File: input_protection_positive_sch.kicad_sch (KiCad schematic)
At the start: 25 parts, among them Q1 SQM120P06, Q2 SQM120P06, U1 ADM1270

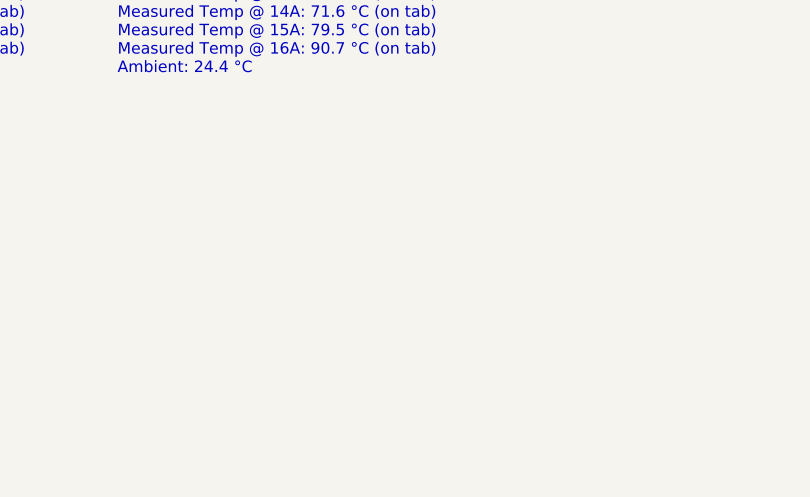
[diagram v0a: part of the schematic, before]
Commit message: Only run pre-commit hooks in the datasheet dir
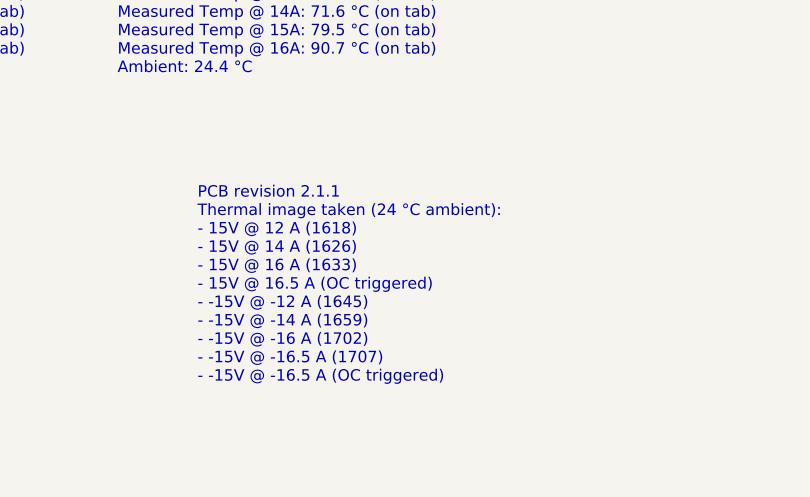
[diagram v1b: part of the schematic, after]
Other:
- note added: "PCB revision 2.1.1 Thermal image taken (24 °C ambient): - 15V @ 12 A (1618) - 15V @ 14 A (1626) - 15V @ 16 A (1633) - 15V @ 16.5 A (OC triggered) - -15V @ -12 A (1645) - -15V @ -14 A (1659) - -15V @ -16 A (1702) - -15V @ -16.5 A (1707) - -15V @ -16.5 A (OC triggered)"
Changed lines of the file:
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@@
+		)
+	)
+	(text "PCB revision 2.1.1\nThermal image taken (24 °C ambient):\n- 15V @ 12 A (1618)\n- 15V @ 14 A (1626)\n- 15V @ 16 A (1633)\n- 15V @ 16.5 A (OC triggered)\n- -15V @ -12 A (1645)\n- -15V @ -14 A (1659)\n- -15V @ -16 A (1702)\n- -15V @ -16.5 A (1707)\n- -15V @ -16.5 A (OC triggered)"
+		(exclude_from_sim no)
+		(at 101.6 180.34 0)
+		(effects
+			(font
+				(size 1.27 1.27)
+			)
+			(justify left bottom)
 		)
 	)

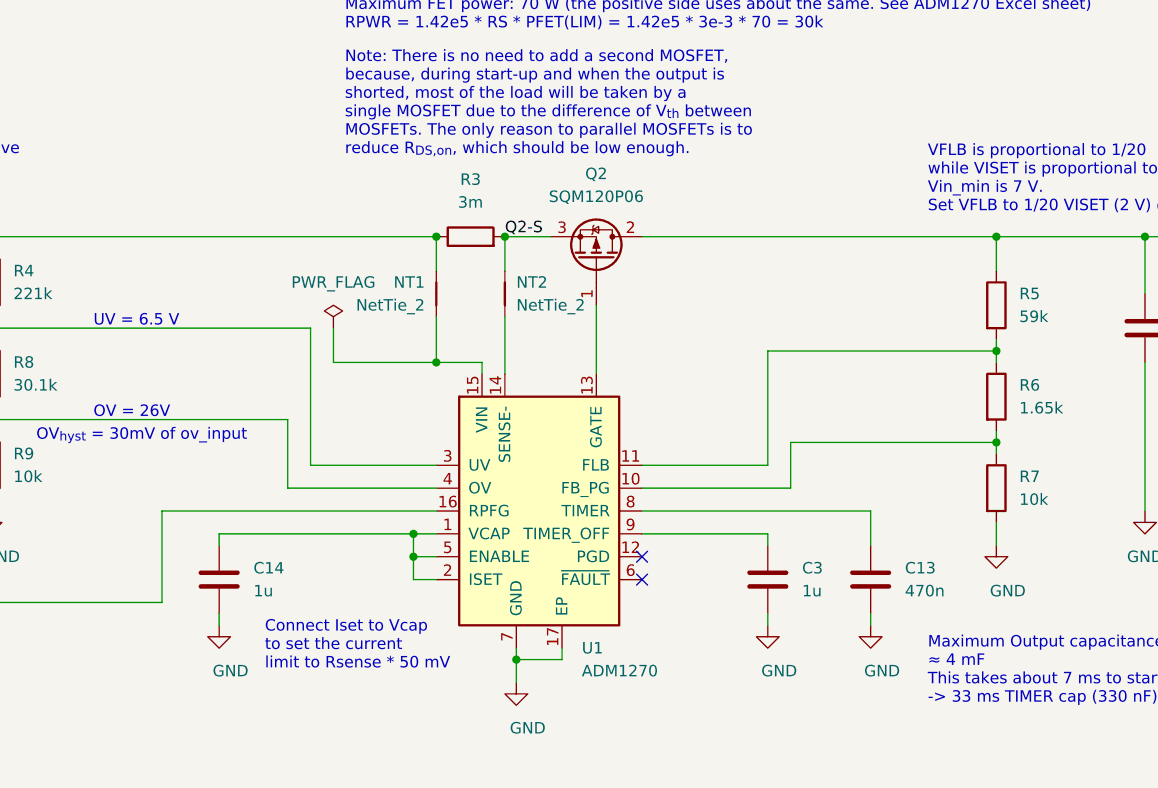
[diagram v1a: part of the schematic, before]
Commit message: Updated libraries
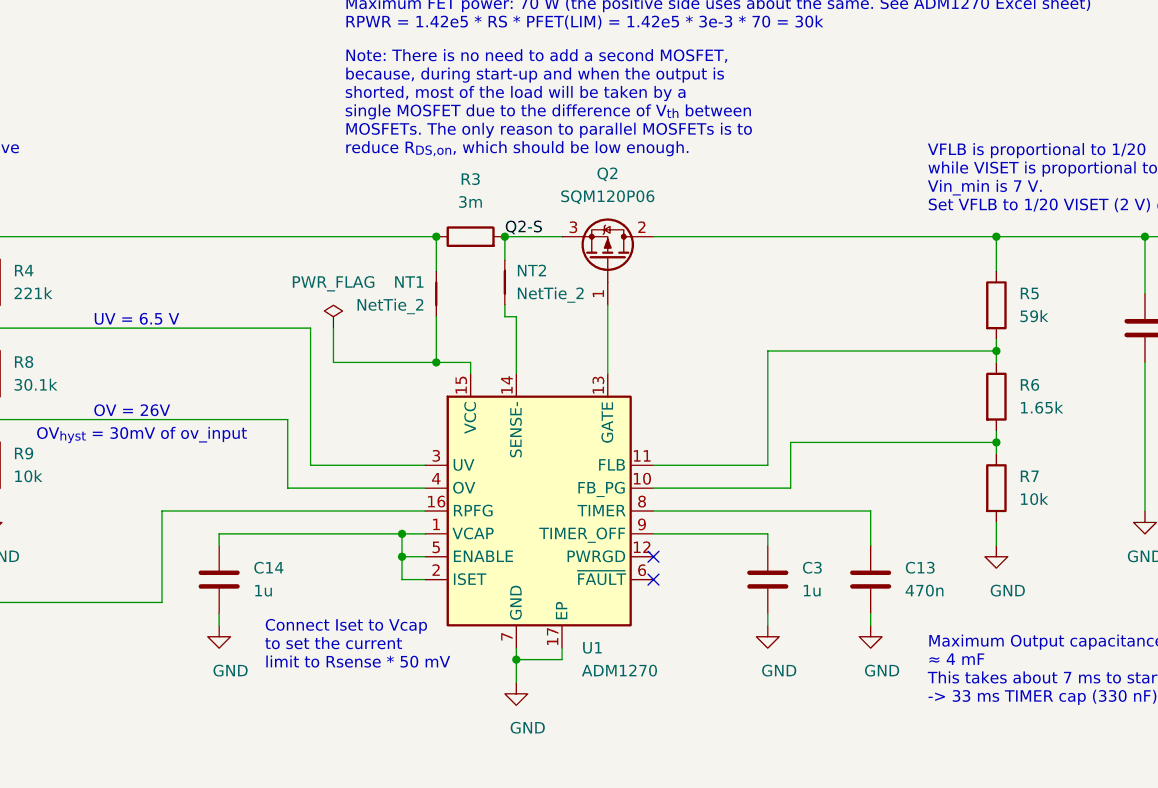
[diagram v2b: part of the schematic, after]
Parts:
- U1: footprint Package_DFN_QFN:QFN-16-1EP_3x3mm_P0.5mm_EP1.45x1.45mm -> Package_CSP:LFCSP-16-1EP_3x3mm_P0.5mm_EP1.5x1.5mm; symbol ADI:ADM1270ACPZ -> Power_Management:ADM1270ACPZ
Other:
- moved on the sheet: NT2, Q2
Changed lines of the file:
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@@
 	)
 	(junction
-		(at 163.83 100.33)
+		(at 162.56 100.33)
 		(diameter 0)
 		(color 0 0 0 0)
@@
 	)
 	(junction
-		(at 163.83 97.79)
+		(at 162.56 97.79)
 		(diameter 0)
 		(color 0 0 0 0)
@@
 	)
 	(no_connect
-		(at 189.23 102.87)
+		(at 190.5 102.87)
 	)
 	(no_connect
-		(at 189.23 100.33)
+		(at 190.5 100.33)
 	)
 	(wire
 		(pts
-			(xy 163.83 100.33) (xy 163.83 102.87)
+			(xy 162.56 100.33) (xy 162.56 102.87)
 		)
 		(stroke
@@
 	(wire
 		(pts
-			(xy 189.23 97.79) (xy 203.2 97.79)
+			(xy 190.5 97.79) (xy 203.2 97.79)
 		)
 		(stroke
@@
 	(wire
 		(pts
-			(xy 163.83 102.87) (xy 166.37 102.87)
+			(xy 162.56 102.87) (xy 165.1 102.87)
 		)
 		(stroke
@@
 	(wire
 		(pts
-			(xy 173.99 64.77) (xy 173.99 68.58)
+			(xy 173.99 64.77) (xy 173.99 67.31)
 		)
 		(stroke
@@
 	(wire
 		(pts
-			(xy 163.83 97.79) (xy 163.83 100.33)
+			(xy 162.56 97.79) (xy 162.56 100.33)
 		)
 		(stroke
@@
 	(wire
 		(pts
-			(xy 173.99 73.66) (xy 173.99 80.01)
+			(xy 175.26 73.66) (xy 175.26 80.01)
 		)
 		(stroke
@@
 	(wire
 		(pts
-			(xy 166.37 92.71) (xy 149.86 92.71)
+			(xy 165.1 92.71) (xy 149.86 92.71)
 		)
 		(stroke
@@
 	(wire
 		(pts
+			(xy 175.26 73.66) (xy 173.99 73.66)
+		)
+		(stroke
+			(width 0)
+			(type default)
+		)
+	)
+	(wire
+		(pts
 			(xy 149.86 85.09) (xy 116.84 85.09)
 		)
@@
 	(wire
 		(pts
-			(xy 189.23 95.25) (xy 214.63 95.25)
+			(xy 190.5 95.25) (xy 214.63 95.25)
 		)
 		(stroke
@@
 	(wire
 		(pts
-			(xy 142.24 97.79) (xy 163.83 97.79)
+			(xy 142.24 97.79) (xy 162.56 97.79)
 		)
 		(stroke
@@
 	(wire
 		(pts
-			(xy 166.37 78.74) (xy 171.45 78.74)
+			(xy 166.37 78.74) (xy 170.18 78.74)
 		)
 		(stroke
@@
 	(wire
 		(pts
-			(xy 166.37 100.33) (xy 163.83 100.33)
+			(xy 165.1 100.33) (xy 162.56 100.33)
 		)
 		(stroke
@@
 	(wire
 		(pts
-			(xy 259.08 74.93) (xy 259.08 76.2)
+			(xy 170.18 78.74) (xy 170.18 80.01)
 		)
 		(stroke
@@
 	(wire
 		(pts
-			(xy 228.6 64.77) (xy 245.11 64.77)
+			(xy 173.99 73.66) (xy 173.99 72.39)
 		)
 		(stroke
@@
 	(wire
 		(pts
-			(xy 228.6 77.47) (xy 203.2 77.47)
+			(xy 259.08 74.93) (xy 259.08 76.2)
 		)
 		(stroke
@@
 	(wire
 		(pts
-			(xy 166.37 78.74) (xy 154.94 78.74)
+			(xy 228.6 64.77) (xy 245.11 64.77)
 		)
 		(stroke
@@
 	(wire
 		(pts
-			(xy 163.83 97.79) (xy 166.37 97.79)
+			(xy 228.6 77.47) (xy 203.2 77.47)
 		)
 		(stroke
@@
 	(wire
 		(pts
-			(xy 116.84 73.66) (xy 116.84 74.93)
+			(xy 166.37 78.74) (xy 154.94 78.74)
 		)
 		(stroke
@@
 	(wire
 		(pts
-			(xy 203.2 90.17) (xy 189.23 90.17)
+			(xy 162.56 97.79) (xy 165.1 97.79)
 		)
 		(stroke
@@
 	(wire
 		(pts
-			(xy 101.6 74.93) (xy 101.6 73.66)
+			(xy 116.84 73.66) (xy 116.84 74.93)
 		)
 		(stroke
@@
 	(wire
 		(pts
-			(xy 245.11 64.77) (xy 245.11 71.12)
+			(xy 203.2 90.17) (xy 190.5 90.17)
 		)
 		(stroke
@@
 	(wire
 		(pts
-			(xy 99.06 64.77) (xy 101.6 64.77)
+			(xy 101.6 74.93) (xy 101.6 73.66)
 		)
 		(stroke
@@
 	(wire
 		(pts
-			(xy 184.15 72.39) (xy 184.15 80.01)
+			(xy 245.11 64.77) (xy 245.11 71.12)
 		)
 		(stroke
@@
 	(wire
 		(pts
-			(xy 166.37 64.77) (xy 166.37 68.58)
+			(xy 99.06 64.77) (xy 101.6 64.77)
 		)
 		(stroke
@@
 	(wire
 		(pts
-			(xy 228.6 86.36) (xy 228.6 87.63)
+			(xy 166.37 64.77) (xy 166.37 68.58)
 		)
 		(stroke
@@
 	(wire
 		(pts
-			(xy 171.45 78.74) (xy 171.45 80.01)
+			(xy 228.6 86.36) (xy 228.6 87.63)
 		)
 		(stroke
@@
 	(wire
 		(pts
-			(xy 135.89 95.25) (xy 166.37 95.25)
+			(xy 135.89 95.25) (xy 165.1 95.25)
 		)
 		(stroke
@@
 	(wire
 		(pts
-			(xy 166.37 90.17) (xy 152.4 90.17)
+			(xy 165.1 90.17) (xy 152.4 90.17)
 		)
 		(stroke
@@
 	(wire
 		(pts
-			(xy 189.23 64.77) (xy 228.6 64.77)
+			(xy 190.5 64.77) (xy 228.6 64.77)
 		)
 		(stroke
@@
 	(wire
 		(pts
-			(xy 189.23 92.71) (xy 205.74 92.71)
+			(xy 185.42 72.39) (xy 185.42 80.01)
+		)
+		(stroke
+			(width 0)
+			(type default)
+		)
+	)
+	(wire
+		(pts
+			(xy 190.5 92.71) (xy 205.74 92.71)
 		)
 		(stroke
@@
 	(wire
 		(pts
-			(xy 173.99 64.77) (xy 179.07 64.77)
+			(xy 173.99 64.77) (xy 180.34 64.77)
 		)
 		(stroke
@@
 	(symbol
 		(lib_id "Device:NetTie_2")
-		(at 173.99 71.12 90)
+		(at 173.99 69.85 90)
 		(unit 1)
 		(exclude_from_sim no)
@@
 		(dnp no)
 		(property "Reference" "NT2"
-			(at 175.26 69.85 90)
+			(at 175.26 68.58 90)
 			(effects
 				(font
@@
 		)
 		(property "Value" "NetTie_2"
-			(at 175.26 72.39 90)
+			(at 175.26 71.12 90)
 			(effects
 				(font
@@
 		)
 		(property "Footprint" "Custom_footprints:NET-TIE-0.20mm"
-			(at 173.99 71.12 0)
+			(at 173.99 69.85 0)
 			(effects
 				(font
@@
 		)
 		(property "Datasheet" "~"
-			(at 173.99 71.12 0)
+			(at 173.99 69.85 0)
 			(effects
 				(font
@@
 		)
 		(property "Description" ""
-			(at 173.99 71.12 0)
+			(at 173.99 69.85 0)
 			(effects
 				(font
@@
 		)
 		(property "MFN" ""
-			(at 173.99 71.12 0)
+			(at 173.99 69.85 0)
 			(effects
 				(font
@@
 		)
 		(property "PN" ""
-			(at 173.99 71.12 0)
+			(at 173.99 69.85 0)
 			(effects
 				(font
@@
 		)
 		(property "RoHS" ""
-			(at 173.99 71.12 0)
+			(at 173.99 69.85 0)
 			(effects
 				(font
@@
 	(symbol
 		(lib_id "Device:Q_PMOS_GDS")
-		(at 184.15 67.31 270)
+		(at 185.42 67.31 270)
 		(mirror x)
 		(unit 1)
@@
 		(dnp no)
 		(property "Reference" "Q2"
-			(at 184.15 57.785 90)
+			(at 185.42 57.785 90)
 			(effects
 				(font
@@
 		)
 		(property "Value" "SQM120P06"
-			(at 184.15 60.325 90)
+			(at 185.42 60.325 90)
 			(effects
 				(font
@@
 		)
 		(property "Footprint" "Package_TO_SOT_SMD:TO-263-2"
-			(at 186.69 62.23 0)
+			(at 187.96 62.23 0)
 			(effects
 				(font
@@
 		)
 		(property "Datasheet" "~"
-			(at 184.15 67.31 0)
+			(at 185.42 67.31 0)
 			(effects
 				(font
@@
 		)
 		(property "Description" ""
-			(at 184.15 67.31 0)
+			(at 185.42 67.31 0)
 			(effects
 				(font
@@
 		)
 		(property "MFN" "Vishay"
-			(at 184.15 67.31 0)
+			(at 185.42 67.31 0)
 			(effects
 				(font
@@
 		)
 		(property "PN" "SQM120P06-07L_GE3"
-			(at 184.15 67.31 0)
+			(at 185.42 67.31 0)
 			(effects
 				(font
@@
 		)
 		(property "Temperature" "Tstorage = –75 °C to 175 °C"
-			(at 184.15 67.31 0)
+			(at 185.42 67.31 0)
 			(effects
 				(font
@@
 		)
 		(property "RoHS" "By exemption"
-			(at 184.15 67.31 0)
+			(at 185.42 67.31 0)
 			(effects
 				(font
@@
 		)
 		(property "Note" "Vds >= 60V"
-			(at 184.15 67.31 0)
+			(at 185.42 67.31 0)
 			(effects
 				(font
@@
 	)
 	(symbol
-		(lib_id "ADI:ADM1270ACPZ")
+		(lib_id "Power_Management:ADM1270ACPZ")
 		(at 177.8 95.25 0)
 		(unit 1)
@@
 			)
 		)
-		(property "Footprint" "Package_DFN_QFN:QFN-16-1EP_3x3mm_P0.5mm_EP1.45x1.45mm"
+		(property "Footprint" "Package_CSP:LFCSP-16-1EP_3x3mm_P0.5mm_EP1.5x1.5mm"
 			(at 181.61 110.49 0)
 			(effects
@@
 			)
 		)
-		(property "Description" ""
-			(at 177.8 95.25 0)
+		(property "Description" "High Voltage Input Protection Device"
+			(at 179.07 95.25 0)
 			(effects
 				(font
